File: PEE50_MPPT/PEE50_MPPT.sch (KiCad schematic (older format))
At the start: 46 parts, among them J1 PV_IN1, J2 PV_IN2, J3 Conn_01x02_Female, J4 Conn_01x02_Female, J5 PV_IN4, J6 PV_IN3, Q1 BC547, Q2 BC547, Q3 BC547, Q4 BC547, U1 LM3480-3.3

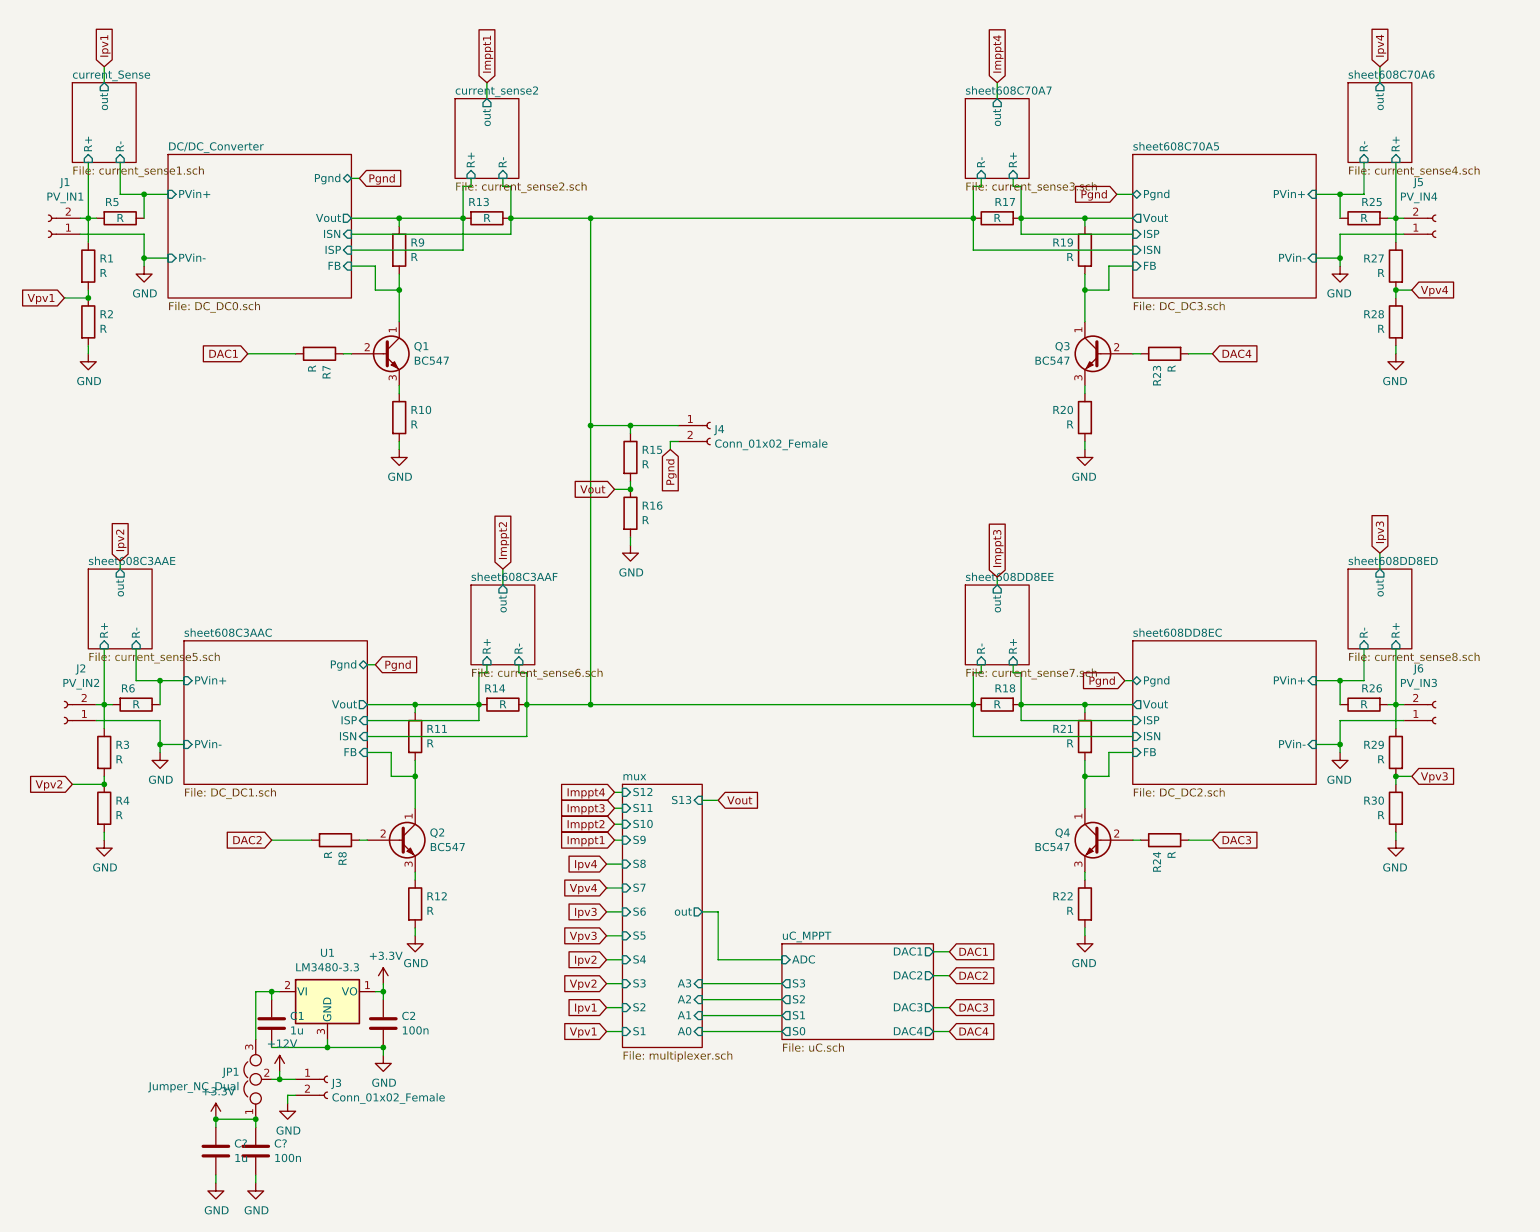
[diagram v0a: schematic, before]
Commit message: weerstand waardes ingevoegd
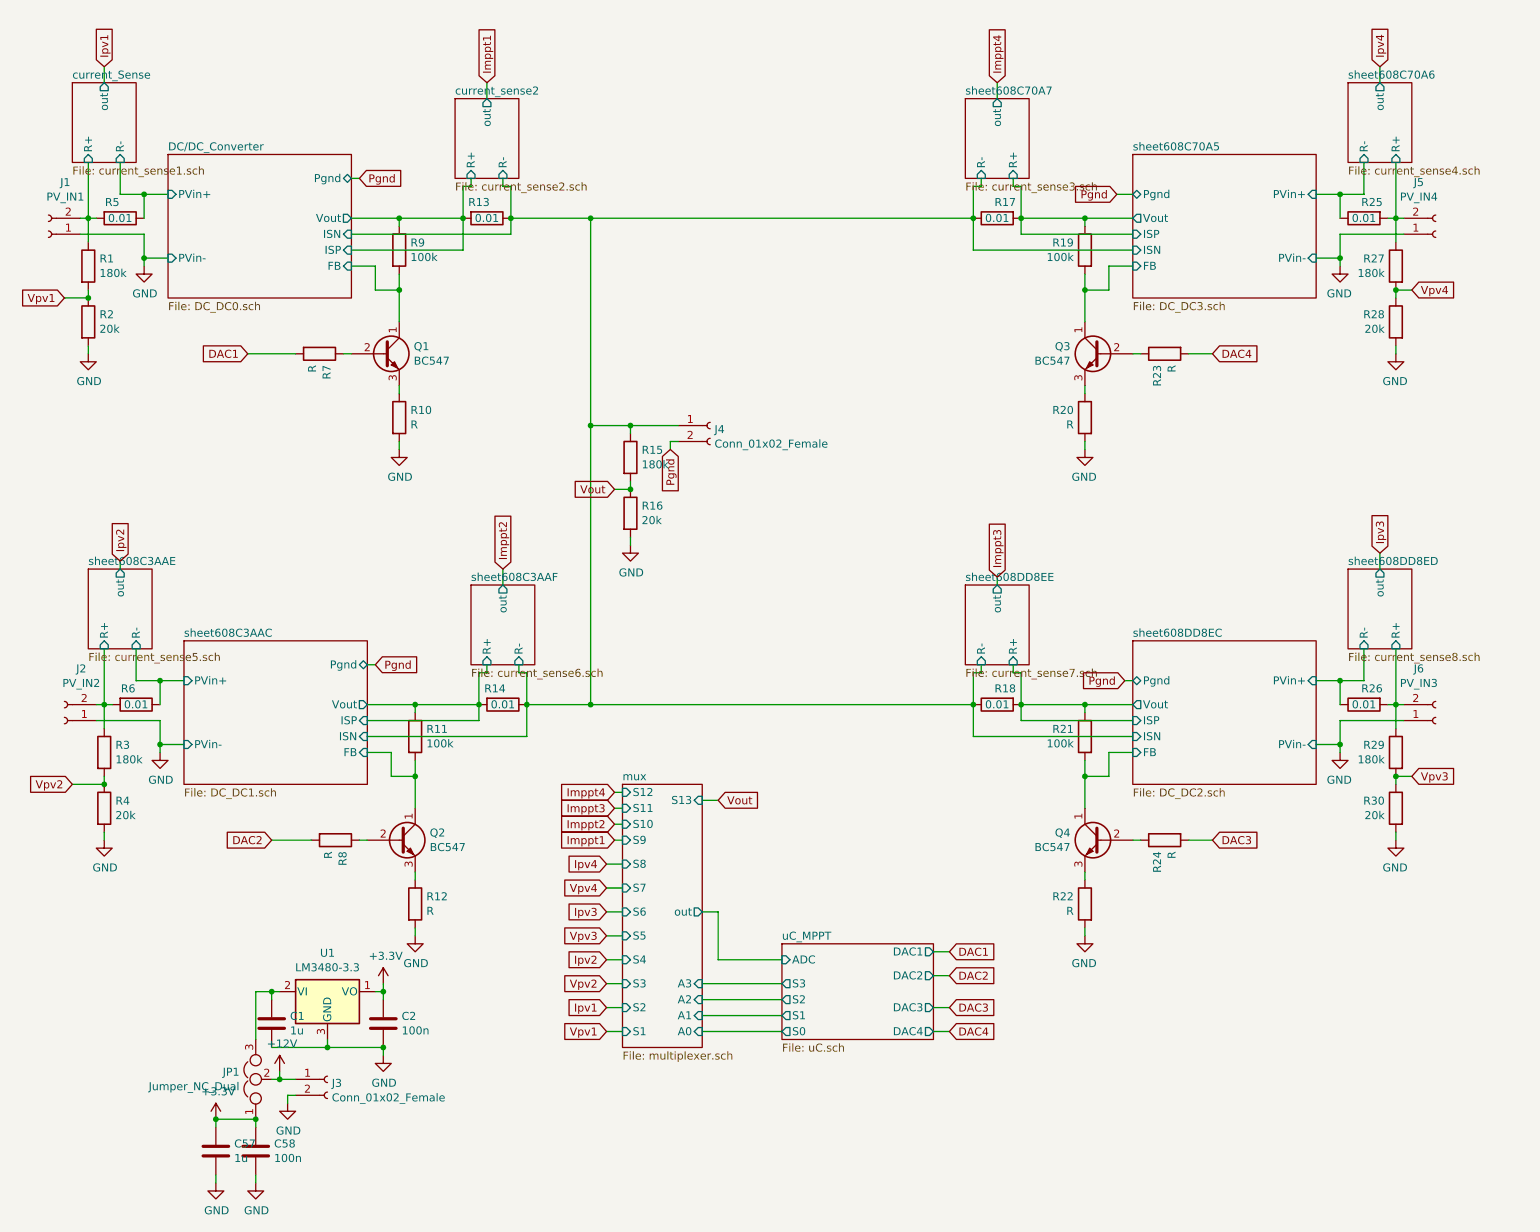
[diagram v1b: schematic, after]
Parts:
- R1, R15, R27, R29, R3: value R -> 180k
- R11, R19, R21, R9: value R -> 100k
- R13, R14, R17, R18, R25, R26, R5, R6: value R -> 0.01
- R16, R2, R28, R30, R4: value R -> 20k
- gave numbers to parts that had none: 2
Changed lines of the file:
@@
 P 2900 1950
 F 0 "R9" H 2970 1996 50  0000 L CNN
-F 1 "R" H 2970 1905 50  0000 L CNN
+F 1 "100k" H 2970 1905 50  0000 L CNN
 F 2 "" V 2830 1950 50  0001 C CNN
 F 3 "~" H 2900 1950 50  0001 C CNN
@@
 P 1150 1750
 F 0 "R5" V 1050 1700 50  0000 C CNN
-F 1 "R" V 1150 1750 50  0000 C CNN
+F 1 "0.01" V 1150 1750 50  0000 C CNN
 F 2 "" V 1080 1750 50  0001 C CNN
 F 3 "~" H 1150 1750 50  0001 C CNN
@@
 P 3450 1750
 F 0 "R13" V 3350 1700 50  0000 C CNN
-F 1 "R" V 3450 1750 50  0000 C CNN
+F 1 "0.01" V 3450 1750 50  0000 C CNN
 F 2 "" V 3380 1750 50  0001 C CNN
 F 3 "~" H 3450 1750 50  0001 C CNN
@@
 P 950 2050
 F 0 "R1" H 1020 2096 50  0000 L CNN
-F 1 "R" H 1020 2005 50  0000 L CNN
+F 1 "180k" H 1020 2005 50  0000 L CNN
 F 2 "" V 880 2050 50  0001 C CNN
 F 3 "~" H 950 2050 50  0001 C CNN
@@
 P 950 2400
 F 0 "R2" H 1020 2446 50  0000 L CNN
-F 1 "R" H 1020 2355 50  0000 L CNN
+F 1 "20k" H 1020 2355 50  0000 L CNN
 F 2 "" V 880 2400 50  0001 C CNN
 F 3 "~" H 950 2400 50  0001 C CNN
@@
 P 4350 3250
 F 0 "R15" H 4420 3296 50  0000 L CNN
-F 1 "R" H 4420 3205 50  0000 L CNN
+F 1 "180k" H 4420 3205 50  0000 L CNN
 F 2 "" V 4280 3250 50  0001 C CNN
 F 3 "~" H 4350 3250 50  0001 C CNN
@@
 P 4350 3600
 F 0 "R16" H 4420 3646 50  0000 L CNN
-F 1 "R" H 4420 3555 50  0000 L CNN
+F 1 "20k" H 4420 3555 50  0000 L CNN
 F 2 "" V 4280 3600 50  0001 C CNN
 F 3 "~" H 4350 3600 50  0001 C CNN
@@
 P 3000 5000
 F 0 "R11" H 3070 5046 50  0000 L CNN
-F 1 "R" H 3070 4955 50  0000 L CNN
+F 1 "100k" H 3070 4955 50  0000 L CNN
 F 2 "" V 2930 5000 50  0001 C CNN
 F 3 "~" H 3000 5000 50  0001 C CNN
@@
 Wire Wire Line
 	3000 5850 3000 5900
-$Comp
-L power:GND #PWR010
-U 1 1 608C3ADC
-P 3000 6250
-F 0 "#PWR010" H 3000 6000 50  0001 C CNN
-F 1 "GND" H 3005 6077 50  0000 C CNN
-F 2 "" H 3000 6250 50  0001 C CNN
-F 3 "" H 3000 6250 50  0001 C CNN
-	1    3000 6250
-	1    0    0    -1
-$EndComp
-Wire Wire Line
-	3000 6200 3000 6250
 $Comp
 L power:GND #PWR04
@@
 P 1250 4800
 F 0 "R6" V 1150 4750 50  0000 C CNN
-F 1 "R" V 1250 4800 50  0000 C CNN
+F 1 "0.01" V 1250 4800 50  0000 C CNN
 F 2 "" V 1180 4800 50  0001 C CNN
 F 3 "~" H 1250 4800 50  0001 C CNN
@@
 P 3550 4800
 F 0 "R14" V 3450 4750 50  0000 C CNN
-F 1 "R" V 3550 4800 50  0000 C CNN
+F 1 "0.01" V 3550 4800 50  0000 C CNN
 F 2 "" V 3480 4800 50  0001 C CNN
 F 3 "~" H 3550 4800 50  0001 C CNN
@@
 P 1050 5100
 F 0 "R3" H 1120 5146 50  0000 L CNN
-F 1 "R" H 1120 5055 50  0000 L CNN
+F 1 "180k" H 1120 5055 50  0000 L CNN
 F 2 "" V 980 5100 50  0001 C CNN
 F 3 "~" H 1050 5100 50  0001 C CNN
@@
 P 1050 5450
 F 0 "R4" H 1120 5496 50  0000 L CNN
-F 1 "R" H 1120 5405 50  0000 L CNN
+F 1 "20k" H 1120 5405 50  0000 L CNN
 F 2 "" V 980 5450 50  0001 C CNN
 F 3 "~" H 1050 5450 50  0001 C CNN
@@
 P 7200 1950
 F 0 "R19" H 7270 1996 50  0000 L CNN
-F 1 "R" H 7270 1905 50  0000 L CNN
+F 1 "100k" H 7270 1905 50  0000 L CNN
 F 2 "" V 7130 1950 50  0001 C CNN
 F 3 "~" H 7200 1950 50  0001 C CNN
@@
 	-1   0    0    -1
 $EndComp
-Wire Wire Line
-	7200 3150 7200 3200
 $Comp
 L power:GND #PWR014
@@
 P 8950 1750
 F 0 "R25" V 8850 1700 50  0000 C CNN
-F 1 "R" V 8950 1750 50  0000 C CNN
+F 1 "0.01" V 8950 1750 50  0000 C CNN
 F 2 "" V 8880 1750 50  0001 C CNN
 F 3 "~" H 8950 1750 50  0001 C CNN
@@
 P 6650 1750
 F 0 "R17" V 6550 1700 50  0000 C CNN
-F 1 "R" V 6650 1750 50  0000 C CNN
+F 1 "0.01" V 6650 1750 50  0000 C CNN
 F 2 "" V 6580 1750 50  0001 C CNN
 F 3 "~" H 6650 1750 50  0001 C CNN
@@
 P 9150 2050
 F 0 "R27" H 9220 2096 50  0000 L CNN
-F 1 "R" H 9220 2005 50  0000 L CNN
+F 1 "180k" H 9220 2005 50  0000 L CNN
 F 2 "" V 9080 2050 50  0001 C CNN
 F 3 "~" H 9150 2050 50  0001 C CNN
@@
 P 9150 2400
 F 0 "R28" H 9220 2446 50  0000 L CNN
-F 1 "R" H 9220 2355 50  0000 L CNN
+F 1 "20k" H 9220 2355 50  0000 L CNN
 F 2 "" V 9080 2400 50  0001 C CNN
 F 3 "~" H 9150 2400 50  0001 C CNN
@@
 P 7200 5000
 F 0 "R21" H 7270 5046 50  0000 L CNN
-F 1 "R" H 7270 4955 50  0000 L CNN
+F 1 "100k" H 7270 4955 50  0000 L CNN
 F 2 "" V 7130 5000 50  0001 C CNN
 F 3 "~" H 7200 5000 50  0001 C CNN
@@
 	-1   0    0    -1
 $EndComp
-Wire Wire Line
-	7200 6200 7200 6250
 $Comp
 L power:GND #PWR015
@@
 P 8950 4800
 F 0 "R26" V 8850 4750 50  0000 C CNN
-F 1 "R" V 8950 4800 50  0000 C CNN
+F 1 "0.01" V 8950 4800 50  0000 C CNN
 F 2 "" V 8880 4800 50  0001 C CNN
 F 3 "~" H 8950 4800 50  0001 C CNN
@@
 P 6650 4800
 F 0 "R18" V 6550 4750 50  0000 C CNN
-F 1 "R" V 6650 4800 50  0000 C CNN
+F 1 "0.01" V 6650 4800 50  0000 C CNN
 F 2 "" V 6580 4800 50  0001 C CNN
 F 3 "~" H 6650 4800 50  0001 C CNN
@@
 P 9150 5100
 F 0 "R29" H 9220 5146 50  0000 L CNN
-F 1 "R" H 9220 5055 50  0000 L CNN
+F 1 "180k" H 9220 5055 50  0000 L CNN
 F 2 "" V 9080 5100 50  0001 C CNN
 F 3 "~" H 9150 5100 50  0001 C CNN
@@
 P 9150 5450
 F 0 "R30" H 9220 5496 50  0000 L CNN
-F 1 "R" H 9220 5405 50  0000 L CNN
+F 1 "20k" H 9220 5405 50  0000 L CNN
 F 2 "" V 9080 5450 50  0001 C CNN
 F 3 "~" H 9150 5450 50  0001 C CNN
@@
 	2150 7150 2250 7150
 $Comp
-L Device:C C?
+L Device:C C57
 U 1 1 609BC7B7
 P 1750 7600
-F 0 "C?" H 1865 7646 50  0000 L CNN
+F 0 "C57" H 1865 7646 50  0000 L CNN
 F 1 "1u" H 1865 7555 50  0000 L CNN
 F 2 "" H 1788 7450 50  0001 C CNN
@@
 $EndComp
 $Comp
-L Device:C C?
+L Device:C C58
 U 1 1 609BC825
 P 2000 7600
-F 0 "C?" H 2115 7646 50  0000 L CNN
+F 0 "C58" H 2115 7646 50  0000 L CNN
 F 1 "100n" H 2115 7555 50  0000 L CNN
 F 2 "" H 2038 7450 50  0001 C CNN
@@
 Connection ~ 1750 7400
 $Comp
-L power:GND #PWR?
+L power:GND #PWR0102
 U 1 1 609D5787
 P 2000 7800
-F 0 "#PWR?" H 2000 7550 50  0001 C CNN
+F 0 "#PWR0102" H 2000 7550 50  0001 C CNN
 F 1 "GND" H 2005 7627 50  0000 C CNN
 F 2 "" H 2000 7800 50  0001 C CNN
@@
 $EndComp
 $Comp
-L power:GND #PWR?
+L power:GND #PWR0103
 U 1 1 609D57EE
 P 1750 7800
-F 0 "#PWR?" H 1750 7550 50  0001 C CNN
+F 0 "#PWR0103" H 1750 7550 50  0001 C CNN
 F 1 "GND" H 1755 7627 50  0000 C CNN
 F 2 "" H 1750 7800 50  0001 C CNN
@@
 Wire Wire Line
 	2000 7800 2000 7750
+Wire Wire Line
+	7200 6200 7200 6250
+Wire Wire Line
+	7200 3150 7200 3200
+Wire Wire Line
+	3000 6200 3000 6250
+$Comp
+L power:GND #PWR010
+U 1 1 608C3ADC
+P 3000 6250
+F 0 "#PWR010" H 3000 6000 50  0001 C CNN
+F 1 "GND" H 3005 6077 50  0000 C CNN
+F 2 "" H 3000 6250 50  0001 C CNN
+F 3 "" H 3000 6250 50  0001 C CNN
+	1    3000 6250
+	1    0    0    -1
+$EndComp
 $EndSCHEMATC
